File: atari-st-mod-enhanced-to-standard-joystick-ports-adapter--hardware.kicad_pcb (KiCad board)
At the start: 2 copper layers, 45 parts, among them J1 Joy0/Mouse, J2 Joy1, J3 OLED 128×64, J4 Enhanced Joystick Port, J5 Joy0/Mouse, J6 Joy1, Q1 1<Vgsth<2, Low Rdson, Vds >10, Q10 1<Vgsth<2, Low Rdson, Vds >10, Q2 1<Vgsth<2, Low Rdson, Vds >10, Q3 1<Vgsth<2, Low Rdson, Vds >10, Q4 1<Vgsth<2, Low Rdson, Vds >10, Q5 1<Vgsth<2, Low Rdson, Vds >10, Q6 1<Vgsth<2, Low Rdson, Vds >10, Q7 1<Vgsth<2, Low Rdson, Vds >10, Q8 1<Vgsth<2, Low Rdson, Vds >10, Q9 1<Vgsth<2, Low Rdson, Vds >10, SW1 Reset, SW2 Selector, SW3 Activate/Change, SW4 Cancel, U1 LM4040DBZ-3

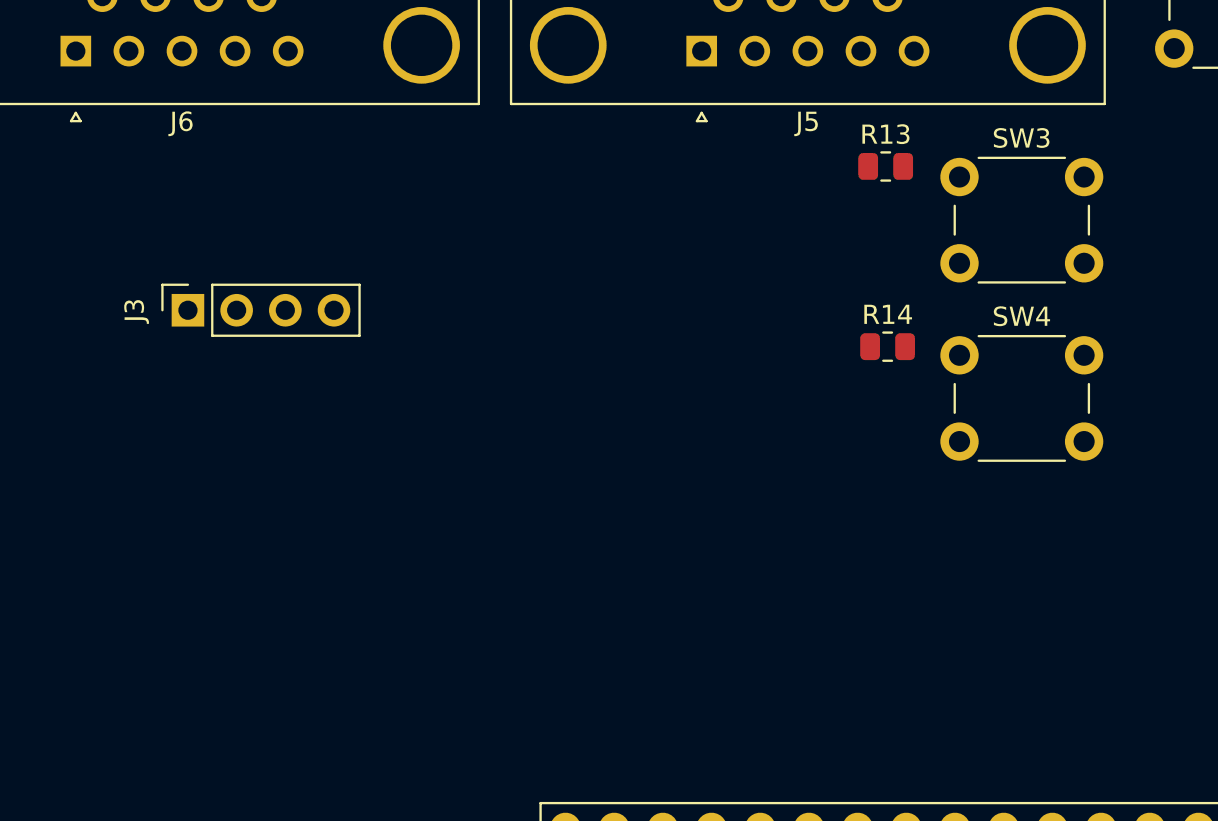
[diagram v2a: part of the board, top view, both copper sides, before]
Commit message: replace basic pin header connector by proper footprint for oled screen
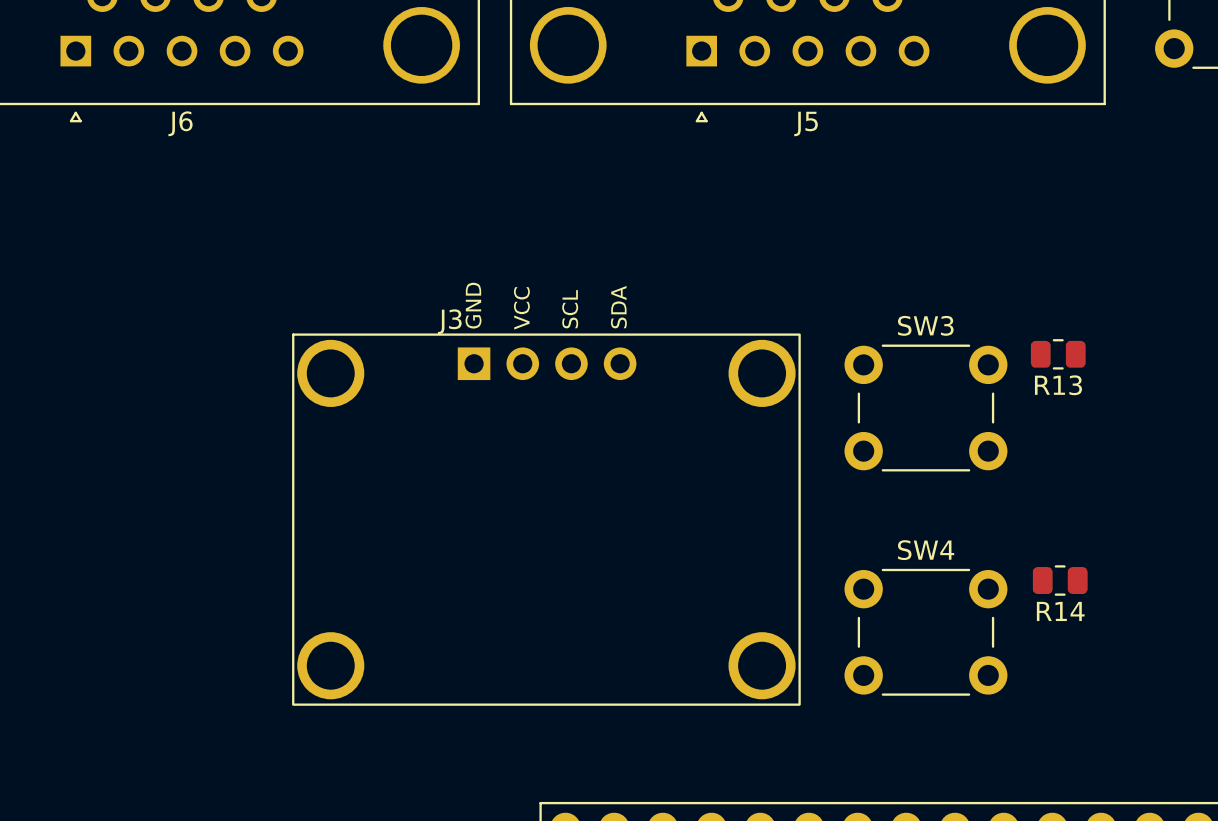
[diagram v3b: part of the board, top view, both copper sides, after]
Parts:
- J3: footprint Connector_PinSocket_2.54mm:PinSocket_1x04_P2.54mm_Vertical -> assemblies_displays_oled:oled_display_iic_128x64pix__outer_26.70x19.26mm__inner_21.74x11.2mm
- moved J3 18.9 mm to (98.7, 74.1), turned to 0 degrees
- moved R14 15.2 mm to (125.5, 85.4), turned to 180 degrees
- moved R13 13.3 mm to (125.4, 73.6), turned to 180 degrees
- moved SW4 13.2 mm to (115.2, 85.8)
- moved SW3 11.0 mm to (115.2, 74.2)
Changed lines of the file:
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@@
   )
   (footprint "Button_Switch_THT:SW_PUSH_6mm_H13mm" (layer "F.Cu")
-    (at 120.25 73.65)
+    (at 115.25 85.85)
     (descr "tactile push button, 6x6mm e.g. PHAP33xx series, height=13mm")
     (tags "tact sw push 6mm")
@@
     )
   )
-  (footprint "Connector_PinSocket_2.54mm:PinSocket_1x04_P2.54mm_Vertical" (layer "F.Cu")
-    (at 80 71.3 90)
-    (descr "Through hole straight socket strip, 1x04, 2.54mm pitch, single row (from Kicad 4.0.7), script generated")
-    (tags "Through hole socket strip THT 1x04 2.54mm single row")
+  (footprint "assemblies_displays_oled:oled_display_iic_128x64pix__outer_26.70x19.26mm__inner_21.74x11.2mm" (layer "F.Cu")
+    (at 98.7 74.0942)
+    (descr "Through hole straight pin header, 1x04, 2.54mm pitch, single row")
+    (tags "Through hole pin header THT 1x04 2.54mm single row")
     (property "Sheetfile" "atari-st-mod-enhanced-to-standard-joystick-ports-adapter--hardware.kicad_sch")
     (property "Sheetname" "")
     (attr through_hole)
-    (fp_text reference "J3" (at 0 -2.77 90) (layer "F.SilkS")
-      (effects (font (size 1 1) (thickness 0.15)))
-    )
-    (fp_text value "OLED 128×64" (at 0 10.39 90) (layer "F.Fab")
-      (effects (font (size 1 1) (thickness 0.15)))
-    )
-    (fp_text user "${REFERENCE}" (at 0 3.81) (layer "F.Fab")
-      (effects (font (size 1 1) (thickness 0.15)))
-    )
-    (fp_line (start -1.33 1.27) (end -1.33 8.95) (layer "F.SilkS") (width 0.12))
-    (fp_line (start -1.33 8.95) (end 1.33 8.95) (layer "F.SilkS") (width 0.12))
-    (fp_line (start -1.33 1.27) (end 1.33 1.27) (layer "F.SilkS") (width 0.12))
-    (fp_line (start 0 -1.33) (end 1.33 -1.33) (layer "F.SilkS") (width 0.12))
-    (fp_line (start 1.33 1.27) (end 1.33 8.95) (layer "F.SilkS") (width 0.12))
-    (fp_line (start 1.33 -1.33) (end 1.33 0) (layer "F.SilkS") (width 0.12))
-    (fp_line (start 1.75 9.4) (end -1.8 9.4) (layer "F.CrtYd") (width 0.05))
-    (fp_line (start -1.8 9.4) (end -1.8 -1.8) (layer "F.CrtYd") (width 0.05))
-    (fp_line (start -1.8 -1.8) (end 1.75 -1.8) (layer "F.CrtYd") (width 0.05))
-    (fp_line (start 1.75 -1.8) (end 1.75 9.4) (layer "F.CrtYd") (width 0.05))
-    (fp_line (start -1.27 8.89) (end -1.27 -1.27) (layer "F.Fab") (width 0.1))
-    (fp_line (start 1.27 -0.635) (end 1.27 8.89) (layer "F.Fab") (width 0.1))
-    (fp_line (start 1.27 8.89) (end -1.27 8.89) (layer "F.Fab") (width 0.1))
-    (fp_line (start -1.27 -1.27) (end 0.635 -1.27) (layer "F.Fab") (width 0.1))
-    (fp_line (start 0.635 -1.27) (end 1.27 -0.635) (layer "F.Fab") (width 0.1))
-    (pad "1" thru_hole rect (at 0 0 90) (size 1.7 1.7) (drill 1) (layers *.Cu *.Mask)
+    (fp_text reference "J3" (at -5.588 -2.286) (layer "F.SilkS")
+      (effects (font (size 1 1) (thickness 0.15)) (justify left))
+    )
+    (fp_text value "OLED 128×64" (at 0 19.05) (layer "F.Fab")
+      (effects (font (size 1 1) (thickness 0.15)))
+    )
+    (fp_text user "SDA" (at 3.81 -1.778 90 unlocked) (layer "F.SilkS")
+      (effects (font (size 0.8 0.8) (thickness 0.15)) (justify left))
+    )
+    (fp_text user "VCC" (at -1.25 -1.778 90 unlocked) (layer "F.SilkS")
+      (effects (font (size 0.8 0.8) (thickness 0.15)) (justify left))
+    )
+    (fp_text user "GND" (at -3.7746 -1.778 90 unlocked) (layer "F.SilkS")
+      (effects (font (size 0.8 0.8) (thickness 0.15)) (justify left))
+    )
+    (fp_text user "SCL" (at 1.27 -1.778 90 unlocked) (layer "F.SilkS")
+      (effects (font (size 0.8 0.8) (thickness 0.15)) (justify left))
+    )
+    (fp_text user "${REFERENCE}" (at 0.0354 -0.0034) (layer "F.Fab")
+      (effects (font (size 1 1) (thickness 0.15)))
+    )
+    (fp_rect (start -13.208 -1.524) (end 13.208 17.78) (layer "F.SilkS") (width 0.12) (fill none))
+    (fp_rect (start -13.35 -1.5) (end 13.35 17.76) (layer "Dwgs.User") (width 0.12) (fill none))
+    (fp_line (start 5.6254 1.7966) (end 5.6254 -1.8034) (layer "F.CrtYd") (width 0.05))
+    (fp_line (start 5.6254 -1.8034) (end -5.5746 -1.8034) (layer "F.CrtYd") (width 0.05))
+    (fp_line (start -5.5746 1.7966) (end 5.6254 1.7966) (layer "F.CrtYd") (width 0.05))
+    (fp_line (start -5.5746 -1.8034) (end -5.5746 1.7966) (layer "F.CrtYd") (width 0.05))
+    (fp_line (start 5.1154 -1.2734) (end 5.1154 1.2666) (layer "F.Fab") (width 0.1))
+    (fp_line (start -4.4096 1.2666) (end -5.0446 0.6316) (layer "F.Fab") (width 0.1))
+    (fp_line (start -5.0446 0.6316) (end -5.0446 -1.2734) (layer "F.Fab") (width 0.1))
+    (fp_line (start -5.0446 -1.2734) (end 5.1154 -1.2734) (layer "F.Fab") (width 0.1))
+    (fp_line (start 5.1154 1.2666) (end -4.4096 1.2666) (layer "F.Fab") (width 0.1))
+    (pad "0" thru_hole circle (at -11.25 0.5) (size 3.5 3.5) (drill 2.5) (layers *.Cu *.Mask))
+    (pad "0" thru_hole circle (at -11.25 15.75) (size 3.5 3.5) (drill 2.5) (layers *.Cu *.Mask))
+    (pad "0" thru_hole circle (at 11.25 15.75) (size 3.5 3.5) (drill 2.5) (layers *.Cu *.Mask))
+    (pad "0" thru_hole circle (at 11.25 0.5) (size 3.5 3.5) (drill 2.5) (layers *.Cu *.Mask))
+    (pad "1" thru_hole rect (at -3.7746 -0.0034 90) (size 1.7 1.7) (drill 1) (layers *.Cu *.Mask)
       (net 3 "GND1") (pinfunction "Pin_1") (pintype "passive"))
-    (pad "2" thru_hole oval (at 0 2.54 90) (size 1.7 1.7) (drill 1) (layers *.Cu *.Mask)
+    (pad "2" thru_hole oval (at -1.2346 -0.0034 90) (size 1.7 1.7) (drill 1) (layers *.Cu *.Mask)
       (net 30 "+3V3") (pinfunction "Pin_2") (pintype "passive"))
-    (pad "3" thru_hole oval (at 0 5.08 90) (size 1.7 1.7) (drill 1) (layers *.Cu *.Mask)
+    (pad "3" thru_hole oval (at 1.3054 -0.0034 90) (size 1.7 1.7) (drill 1) (layers *.Cu *.Mask)
       (net 15 "/oled_scl") (pinfunction "Pin_3") (pintype "passive"))
-    (pad "4" thru_hole oval (at 0 7.62 90) (size 1.7 1.7) (drill 1) (layers *.Cu *.Mask)
+    (pad "4" thru_hole oval (at 3.8454 -0.0034 90) (size 1.7 1.7) (drill 1) (layers *.Cu *.Mask)
       (net 14 "/oled_sda") (pinfunction "Pin_4") (pintype "passive"))
-    (model "${KICAD6_3DMODEL_DIR}/Connector_PinSocket_2.54mm.3dshapes/PinSocket_1x04_P2.54mm_Vertical.wrl"
+    (model "${KICAD6_3DMODEL_DIR}/Connector_PinHeader_2.54mm.3dshapes/PinHeader_1x04_P2.54mm_Vertical.wrl"
       (offset (xyz 0 0 0))
       (scale (xyz 1 1 1))
@@
   )
   (footprint "Button_Switch_THT:SW_PUSH_6mm_H13mm" (layer "F.Cu")
-    (at 120.25 64.35)
+    (at 115.25 74.15)
     (descr "tactile push button, 6x6mm e.g. PHAP33xx series, height=13mm")
     (tags "tact sw push 6mm")
@@
   )
   (footprint "Resistor_SMD:R_0805_2012Metric" (layer "F.Cu")
-    (at 116.4 63.8)
+    (at 125.4 73.6 180)
     (descr "Resistor SMD 0805 (2012 Metric), square (rectangular) end terminal, IPC_7351 nominal, (Body size source: IPC-SM-782 page 72, https://www.pcb-3d.com/wordpress/wp-content/uploads/ipc-sm-782a_amendment_1_and_2.pdf), generated with kicad-footprint-generator")
     (tags "resistor")
@@
     (fp_line (start 1 -0.625) (end 1 0.625) (layer "F.Fab") (width 0.1))
     (fp_line (start -1 0.625) (end -1 -0.625) (layer "F.Fab") (width 0.1))
-    (pad "1" smd roundrect (at -0.9125 0) (size 1.025 1.4) (layers "F.Cu" "F.Paste" "F.Mask") (roundrect_rratio 0.243902)
+    (pad "1" smd roundrect (at -0.9125 0 180) (size 1.025 1.4) (layers "F.Cu" "F.Paste" "F.Mask") (roundrect_rratio 0.243902)
       (net 30 "+3V3") (pintype "passive"))
-    (pad "2" smd roundrect (at 0.9125 0) (size 1.025 1.4) (layers "F.Cu" "F.Paste" "F.Mask") (roundrect_rratio 0.243902)
+    (pad "2" smd roundrect (at 0.9125 0 180) (size 1.025 1.4) (layers "F.Cu" "F.Paste" "F.Mask") (roundrect_rratio 0.243902)
       (net 12 "/button1") (pintype "passive"))
     (model "${KICAD6_3DMODEL_DIR}/Resistor_SMD.3dshapes/R_0805_2012Metric.wrl"
@@
   )
   (footprint "Resistor_SMD:R_0805_2012Metric" (layer "F.Cu")
-    (at 116.5 73.2)
+    (at 125.5 85.4 180)
     (descr "Resistor SMD 0805 (2012 Metric), square (rectangular) end terminal, IPC_7351 nominal, (Body size source: IPC-SM-782 page 72, https://www.pcb-3d.com/wordpress/wp-content/uploads/ipc-sm-782a_amendment_1_and_2.pdf), generated with kicad-footprint-generator")
     (tags "resistor")
@@
     (fp_line (start -1 0.625) (end -1 -0.625) (layer "F.Fab") (width 0.1))
     (fp_line (start 1 0.625) (end -1 0.625) (layer "F.Fab") (width 0.1))
-    (pad "1" smd roundrect (at -0.9125 0) (size 1.025 1.4) (layers "F.Cu" "F.Paste" "F.Mask") (roundrect_rratio 0.243902)
+    (pad "1" smd roundrect (at -0.9125 0 180) (size 1.025 1.4) (layers "F.Cu" "F.Paste" "F.Mask") (roundrect_rratio 0.243902)
       (net 30 "+3V3") (pintype "passive"))
-    (pad "2" smd roundrect (at 0.9125 0) (size 1.025 1.4) (layers "F.Cu" "F.Paste" "F.Mask") (roundrect_rratio 0.243902)
+    (pad "2" smd roundrect (at 0.9125 0 180) (size 1.025 1.4) (layers "F.Cu" "F.Paste" "F.Mask") (roundrect_rratio 0.243902)
       (net 13 "/button2") (pintype "passive"))
     (model "${KICAD6_3DMODEL_DIR}/Resistor_SMD.3dshapes/R_0805_2012Metric.wrl"

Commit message: pcb session 2023-02-08T07:16:02+01:00
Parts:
- added R23: 10K, Resistor_SMD:R_0805_2012Metric, F.Cu at (122.6, 120.6)
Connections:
- net Net-(A1-Pad30) renamed /reset
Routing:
- net /reset: track 0.00 -> 76.7 mm
- net /j1_right: track 0.00 -> 49.8 mm
- net /right1: track 0.00 -> 44.9 mm
- net /left1: track 0.00 -> 42.7 mm
- net /paddle_x: track 0.00 -> 38.0 mm
- net /j1_fire: track 0.00 -> 38.0 mm
- net /jag_row1: track 0.00 -> 37.6 mm
- net /paddle_y: track 0.00 -> 37.4 mm
- net /button1: track 0.00 -> 35.6 mm
- net /jag_col1: track 0.00 -> 31.3 mm
- net /jag_col2: track 0.00 -> 28.0 mm
- net /oled_scl: track 0.00 -> 27.6 mm
- net /oled_sda: track 0.00 -> 27.6 mm
- net /jag_row3: track 0.00 -> 27.6 mm
- net /down1: track 0.00 -> 27.3 mm
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- added copper zone on In1.Cu, net GND
- added copper zone on In2.Cu, net GND2
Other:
- copper layers 2 -> 4

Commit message: pcb session 2023-02-08T21:40:26+01:00
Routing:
- net /j0_fire: track 12.6 -> 197.6 mm, vias 0 -> 1
- net /j0_right: track 13.4 -> 193.4 mm, vias 0 -> 1
- net /j0_down: track 11.2 -> 190.7 mm, vias 0 -> 1
- net /j0_left: track 12.0 -> 191.5 mm, vias 0 -> 1
- net /j0_up: track 10.9 -> 189.5 mm, vias 0 -> 1
- net /j1_fire: track 38.0 -> 207.2 mm, vias 0 -> 1
- net /j1_down: track 11.1 -> 131.8 mm, vias 0 -> 1
- net /j1_left: track 12.0 -> 132.5 mm, vias 0 -> 1
- net /j1_up: track 10.9 -> 130.4 mm, vias 0 -> 1
- net /j1_right: track 49.8 -> 131.7 mm, vias 0 -> 1
- net GND2: vias 0 -> 7
- added copper zone on In1.Cu, net GND1
- added copper zone on In2.Cu, net GND1
- added copper zone on In1.Cu, net GND2

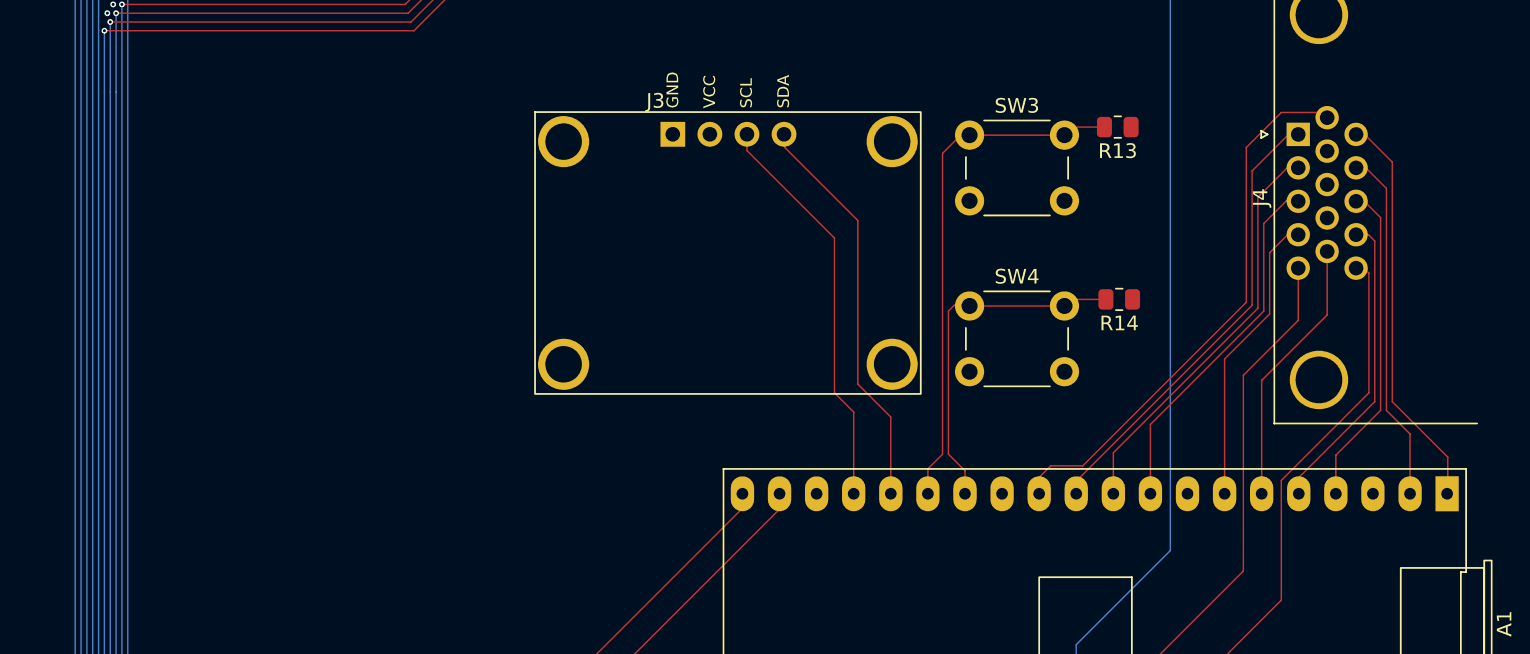
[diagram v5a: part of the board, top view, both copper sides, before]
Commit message: PCB session 2023-02-09T06:26:49+01:00 : title, origin, licence logos, disclaimer on silkscreen
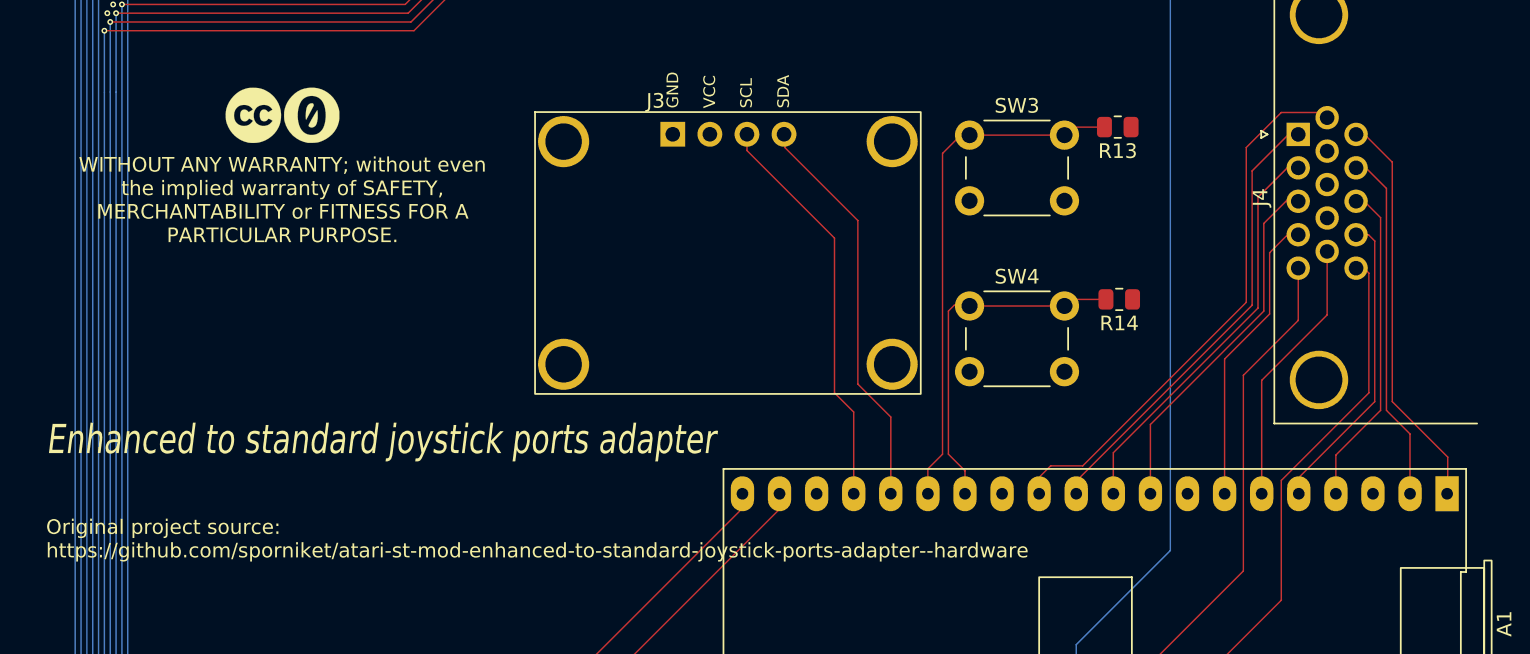
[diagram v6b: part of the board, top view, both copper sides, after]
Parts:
- added G***: LOGO, cliparts:logo--cc--cc, F.Cu at (66.2, 72.8)
- added G***: LOGO, cliparts:logo--cc--zero, F.Cu at (70.2, 72.8)
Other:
- board text added: "Enhanced to standard joystick ports adapter"
- board text added: "Original project source: https://github.com/sporniket/atari-st-mod-enhanced-to-standard-joystick-ports-adapter--hardware"
- board text added: "WITHOUT ANY WARRANTY; without even the implied warranty of SAFETY, MERCHANTABILITY or FITNESS FOR A PARTICULAR PURPOSE."
